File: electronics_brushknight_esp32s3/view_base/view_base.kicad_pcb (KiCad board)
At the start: 4 copper layers, 81.2 x 81.2 mm, 107 parts, among them J1 BLDC, J2 USB_C_Receptacle_USB2.0, J3 LCD, J4 A, J5 B, Q1 MMBT4403, Q2 UMH3N, U1 MT6701-CT, U10 ESP32-S3-WROOM-1-N8R8, U2 CP2102N-A02-GQFN28, U4 HX711, U5 TMC6300, U7 SN74LV1T34DBV, U8 VEML7700, U9 TS1117BCW33_RPG

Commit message: fixed bugs
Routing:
- net /LCD_SCK: track 19.4 -> 17.4 mm, vias 2 -> 1
- net +5V: track 20.2 -> 22.0 mm
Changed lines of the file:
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@@
     (fp_arc (start 3.878787 -15.522725) (mid 3.605918 -15.700082) (end 3.499999 -16.00781)
       (stroke (width 0.2) (type solid)) (layer "B.Fab"))
-    (fp_arc (start 3.878788 -15.522725) (mid 6.302306 -14.706494) (end 8.564827 -13.514574)
+    (fp_arc (start 3.878788 -15.522725) (mid 6.302306 -14.706493) (end 8.564827 -13.514574)
       (stroke (width 0.2) (type solid)) (layer "B.Fab"))
     (fp_arc (start 4.999999 -16.770509) (mid 7.404757 -15.856214) (end 9.649481 -14.599229)
@@
     (fp_arc (start 15.522725 3.878787) (mid 15.700082 3.605918) (end 16.00781 3.499999)
       (stroke (width 0.2) (type solid)) (layer "B.Fab"))
-    (fp_arc (start 15.522725 3.878788) (mid 14.706494 6.302306) (end 13.514574 8.564827)
+    (fp_arc (start 15.522725 3.878788) (mid 14.706493 6.302306) (end 13.514574 8.564827)
       (stroke (width 0.2) (type solid)) (layer "B.Fab"))
     (fp_arc (start 16.007811 -3.5) (mid 15.700077 -3.605911) (end 15.522725 -3.878787)
@@
   (segment (start 65.5 127) (end 72.75 127) (width 0.25) (layer "In1.Cu") (net 37))
   (segment (start 65.5 127) (end 67.5 127) (width 0.25) (layer "B.Cu") (net 37))
-  (via (at 65.5 125) (size 0.8) (drill 0.4) (layers "F.Cu" "B.Cu") (net 38))
   (via (at 77.25 133.5) (size 0.8) (drill 0.4) (layers "F.Cu" "B.Cu") (net 38))
   (segment (start 71.75 125) (end 67.5 125) (width 0.25) (layer "B.Cu") (net 38))
@@
   (segment (start 77.25 133.5) (end 73.25 133.5) (width 0.25) (layer "B.Cu") (net 38))
   (segment (start 72.5 132.75) (end 72.5 125.75) (width 0.25) (layer "B.Cu") (net 38))
-  (segment (start 65.5 125) (end 67.5 125) (width 0.25) (layer "B.Cu") (net 38))
   (segment (start 72.5 125.75) (end 71.75 125) (width 0.25) (layer "B.Cu") (net 38))
   (via (at 77.25 131) (size 0.8) (drill 0.4) (layers "F.Cu" "B.Cu") (net 39))
@@
   (segment (start 93.5 83.57586) (end 93.814763 83.890623) (width 0.65) (layer "F.Cu") (net 81))
   (segment (start 85.825142 88.25) (end 86.431129 88.855987) (width 0.4) (layer "F.Cu") (net 81))
+  (segment (start 69 108.775) (end 68.75 108.525) (width 0.15) (layer "F.Cu") (net 81))
   (segment (start 107.5 83.752753) (end 107.017427 84.235326) (width 0.65) (layer "F.Cu") (net 81))
   (segment (start 114.5 88.5) (end 114.175232 88.5) (width 0.4) (layer "F.Cu") (net 81))
@@
   (segment (start 92.5 116.247247) (end 92.982573 115.764674) (width 0.65) (layer "F.Cu") (net 81))
   (segment (start 106.5 116.42414) (end 106.185237 116.109377) (width 0.65) (layer "F.Cu") (net 81))
+  (segment (start 69 109.4) (end 69 108.775) (width 0.15) (layer "F.Cu") (net 81))
+  (segment (start 69 109.4) (end 69 109.6375) (width 0.15) (layer "F.Cu") (net 81))
   (segment (start 111.5 85.5) (end 111.5 85.825142) (width 0.4) (layer "F.Cu") (net 81))
   (segment (start 88.5 85.824768) (end 89.105236 86.430004) (width 0.4) (layer "F.Cu") (net 81))
@@
   (segment (start 114.5 111.5) (end 114.174858 111.5) (width 0.4) (layer "F.Cu") (net 81))
   (segment (start 111.5 85.825142) (end 110.894013 86.431129) (width 0.4) (layer "F.Cu") (net 81))
+  (segment (start 69 109.6375) (end 68.5875 110.05) (width 0.15) (layer "F.Cu") (net 81))
   (segment (start 85.824768 111.5) (end 86.430004 110.894764) (width 0.4) (layer "F.Cu") (net 81))
   (segment (start 83.25 92.5) (end 83.752753 92.5) (width 0.65) (layer "F.Cu") (net 81))

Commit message: devkit pcb preview
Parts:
- removed D1, D2, D3, D4, D5, D6, D7, D8: SK6812SIDE-A, cleaned footprints:SK6812-SIDE-A
- removed H4: MountHole, Holes:MountingHole_2.2mm_M2_ISO7380_Pad_NonVirtual
- removed Z5: dummy_keepouts, view_custom:ViewKeepouts3d
- added C100: 0.1uF, cleaned footprints:C_0402_1005Metric, F.Cu at (89.3, 122.8)
- added C101: 0.1uF, cleaned footprints:C_0402_1005Metric, F.Cu at (93.5, 124.3)
- added C11: 0.1uF, cleaned footprints:C_0402_1005Metric, F.Cu at (125.1, 97.8)
- added C30: 0.1uF, cleaned footprints:C_0402_1005Metric, F.Cu at (100.0, 125.2)
- added C31: 0.1uF, cleaned footprints:C_0402_1005Metric, F.Cu at (97.8, 74.9)
- added C32: 0.1uF, cleaned footprints:C_0402_1005Metric, F.Cu at (97.8, 125.1)
- added C33: 0.1uF, cleaned footprints:C_0402_1005Metric, F.Cu at (102.2, 74.9)
- added C34: 0.1uF, cleaned footprints:C_0402_1005Metric, F.Cu at (106.5, 124.3)
- added C35: 0.1uF, cleaned footprints:C_0402_1005Metric, F.Cu at (100.0, 74.8)
- added C36: 0.1uF, cleaned footprints:C_0402_1005Metric, F.Cu at (110.7, 122.9)
- added C37: 0.1uF, cleaned footprints:C_0402_1005Metric, F.Cu at (108.6, 76.3)
- added C38: 0.1uF, cleaned footprints:C_0402_1005Metric, F.Cu at (112.6, 78.2)
- added C39: 0.1uF, cleaned footprints:C_0402_1005Metric, F.Cu at (114.5, 120.7)
- added C40: 0.1uF, cleaned footprints:C_0402_1005Metric, F.Cu at (116.2, 80.7)
- added C41: 0.1uF, cleaned footprints:C_0402_1005Metric, F.Cu at (117.8, 117.8)
- added C42: 0.1uF, cleaned footprints:C_0402_1005Metric, F.Cu at (119.3, 83.8)
- added C43: 0.1uF, cleaned footprints:C_0402_1005Metric, F.Cu at (120.7, 114.5)
- added C44: 0.1uF, cleaned footprints:C_0402_1005Metric, F.Cu at (121.8, 87.4)
- added C45: 0.1uF, cleaned footprints:C_0402_1005Metric, F.Cu at (123.7, 91.4)
- added C46: 0.1uF, cleaned footprints:C_0402_1005Metric, F.Cu at (122.8, 110.7)
- added C47: 0.1uF, cleaned footprints:C_0402_1005Metric, F.Cu at (91.4, 76.3)
- added C48: 0.1uF, cleaned footprints:C_0402_1005Metric, F.Cu at (124.3, 106.5)
- added C49: 0.1uF, cleaned footprints:C_0402_1005Metric, F.Cu at (87.4, 78.2)
- added C50: 0.1uF, cleaned footprints:C_0402_1005Metric, F.Cu at (124.8, 104.4)
- added C51: 0.1uF, cleaned footprints:C_0402_1005Metric, F.Cu at (83.8, 80.7)
- added C52: 0.1uF, cleaned footprints:C_0402_1005Metric, F.Cu at (80.7, 83.8)
- added C53: 0.1uF, cleaned footprints:C_0402_1005Metric, F.Cu at (124.3, 93.5)
- added C54: 0.1uF, cleaned footprints:C_0402_1005Metric, F.Cu at (78.2, 87.4)
- added C55: 0.1uF, cleaned footprints:C_0402_1005Metric, F.Cu at (124.8, 95.6)
- added C56: 0.1uF, cleaned footprints:C_0402_1005Metric, F.Cu at (76.3, 91.4)
- added C57: 0.1uF, cleaned footprints:C_0402_1005Metric, F.Cu at (122.8, 89.3)
- added C58: 0.1uF, cleaned footprints:C_0402_1005Metric, F.Cu at (74.9, 97.8)
- added C59: 0.1uF, cleaned footprints:C_0402_1005Metric, F.Cu at (74.9, 102.2)
- added C60: 0.1uF, cleaned footprints:C_0402_1005Metric, F.Cu at (74.8, 100.0)
- added C61: 0.1uF, cleaned footprints:C_0402_1005Metric, F.Cu at (76.3, 108.6)
- added C62: 0.1uF, cleaned footprints:C_0402_1005Metric, F.Cu at (78.2, 112.6)
- added C63: 0.1uF, cleaned footprints:C_0402_1005Metric, F.Cu at (120.7, 85.5)
- added C64: 0.1uF, cleaned footprints:C_0402_1005Metric, F.Cu at (117.8, 82.2)
- added C65: 0.1uF, cleaned footprints:C_0402_1005Metric, F.Cu at (114.5, 79.3)
- added C66: 0.1uF, cleaned footprints:C_0402_1005Metric, F.Cu at (110.7, 77.2)
- added C67: 0.1uF, cleaned footprints:C_0402_1005Metric, F.Cu at (80.7, 116.2)
- added C68: 0.1uF, cleaned footprints:C_0402_1005Metric, F.Cu at (83.8, 119.3)
- added C69: 0.1uF, cleaned footprints:C_0402_1005Metric, F.Cu at (87.4, 121.8)
- added C70: 0.1uF, cleaned footprints:C_0402_1005Metric, F.Cu at (91.4, 123.7)
- added C71: 0.1uF, cleaned footprints:C_0402_1005Metric, F.Cu at (106.5, 75.6)
- added C72: 0.1uF, cleaned footprints:C_0402_1005Metric, F.Cu at (104.4, 75.2)
- added C73: 0.1uF, cleaned footprints:C_0402_1005Metric, F.Cu at (93.5, 75.6)
- added C74: 0.1uF, cleaned footprints:C_0402_1005Metric, F.Cu at (95.6, 75.2)
- added C75: 0.1uF, cleaned footprints:C_0402_1005Metric, F.Cu at (95.6, 124.8)
- added C76: 0.1uF, cleaned footprints:C_0402_1005Metric, F.Cu at (102.2, 125.1)
- added C77: 0.1uF, cleaned footprints:C_0402_1005Metric, F.Cu at (104.4, 124.8)
- added C78: 10uF, smd_clean:C_0603_1608Metric, F.Cu at (114.2, 62.2)
- added C79: 0.1uF, cleaned footprints:C_0402_1005Metric, F.Cu at (89.3, 77.2)
- added C80: 0.1uF, cleaned footprints:C_0402_1005Metric, F.Cu at (85.5, 79.4)
- added C81: 0.1uF, cleaned footprints:C_0402_1005Metric, F.Cu at (82.2, 82.2)
- added C82: 0.1uF, cleaned footprints:C_0402_1005Metric, F.Cu at (79.4, 85.5)
- added C83: 10uF, smd_clean:C_0603_1608Metric, F.Cu at (114.2, 67.3)
- added C84: 100nF, smd_clean:C_0603_1608Metric, F.Cu at (114.2, 68.9)
- added C88: 0.1uF, cleaned footprints:C_0402_1005Metric, F.Cu at (77.2, 89.3)
- added C90: 0.1uF, cleaned footprints:C_0402_1005Metric, F.Cu at (75.7, 93.5)
- added C92: 0.1uF, cleaned footprints:C_0402_1005Metric, F.Cu at (75.2, 95.6)
- added C94: 0.1uF, cleaned footprints:C_0402_1005Metric, F.Cu at (75.2, 104.4)
- added C95: 0.1uF, cleaned footprints:C_0402_1005Metric, F.Cu at (75.6, 106.5)
- added C96: 0.1uF, cleaned footprints:C_0402_1005Metric, F.Cu at (77.2, 110.7)
- added C97: 0.1uF, cleaned footprints:C_0402_1005Metric, F.Cu at (79.3, 114.5)
- added C98: 0.1uF, cleaned footprints:C_0402_1005Metric, F.Cu at (82.2, 117.8)
- added C99: 0.1uF, cleaned footprints:C_0402_1005Metric, F.Cu at (85.5, 120.6)
- added D10: SK6805, cleaned footprints:LED_SK6812_EC15_1.5x1.5mm, F.Cu at (97.7, 126.7)
- added D11: SK6805, cleaned footprints:LED_SK6812_EC15_1.5x1.5mm, F.Cu at (95.3, 126.3)
- added D12: SK6805, cleaned footprints:LED_SK6812_EC15_1.5x1.5mm, F.Cu at (93.1, 125.8)
- added D13: SK6805, cleaned footprints:LED_SK6812_EC15_1.5x1.5mm, F.Cu at (90.8, 125.1)
- added D14: SK6805, cleaned footprints:LED_SK6812_EC15_1.5x1.5mm, F.Cu at (88.7, 124.2)
- added D15: SK6805, cleaned footprints:LED_SK6812_EC15_1.5x1.5mm, F.Cu at (86.6, 123.2)
- added D16: SK6805, cleaned footprints:LED_SK6812_EC15_1.5x1.5mm, F.Cu at (84.7, 121.9)
- added D17: SK6805, cleaned footprints:LED_SK6812_EC15_1.5x1.5mm, F.Cu at (82.8, 120.5)
- added D18: SK6805, cleaned footprints:LED_SK6812_EC15_1.5x1.5mm, F.Cu at (81.1, 118.9)
- added D19: SK6805, cleaned footprints:LED_SK6812_EC15_1.5x1.5mm, F.Cu at (79.5, 117.2)
- added D20: SK6805, cleaned footprints:LED_SK6812_EC15_1.5x1.5mm, F.Cu at (78.1, 115.3)
- added D21: SK6805, cleaned footprints:LED_SK6812_EC15_1.5x1.5mm, F.Cu at (76.8, 113.4)
- added D22: SK6805, cleaned footprints:LED_SK6812_EC15_1.5x1.5mm, F.Cu at (75.8, 111.3)
- added D23: SK6805, cleaned footprints:LED_SK6812_EC15_1.5x1.5mm, F.Cu at (74.9, 109.2)
- added D24: SK6805, cleaned footprints:LED_SK6812_EC15_1.5x1.5mm, F.Cu at (74.2, 106.9)
- added D25: SK6805, cleaned footprints:LED_SK6812_EC15_1.5x1.5mm, F.Cu at (73.7, 104.6)
- added D26: SK6805, cleaned footprints:LED_SK6812_EC15_1.5x1.5mm, F.Cu at (73.4, 102.3)
- added D27: SK6805, cleaned footprints:LED_SK6812_EC15_1.5x1.5mm, F.Cu at (73.2, 100.0)
- added D28: SK6805, cleaned footprints:LED_SK6812_EC15_1.5x1.5mm, F.Cu at (73.4, 97.7)
- added D29: SK6805, cleaned footprints:LED_SK6812_EC15_1.5x1.5mm, F.Cu at (73.7, 95.4)
- added D30: SK6805, cleaned footprints:LED_SK6812_EC15_1.5x1.5mm, F.Cu at (74.2, 93.1)
- added D31: SK6805, cleaned footprints:LED_SK6812_EC15_1.5x1.5mm, F.Cu at (74.9, 90.9)
- added D32: SK6805, cleaned footprints:LED_SK6812_EC15_1.5x1.5mm, F.Cu at (75.8, 88.7)
- added D33: SK6805, cleaned footprints:LED_SK6812_EC15_1.5x1.5mm, F.Cu at (76.8, 86.6)
- added D34: SK6805, cleaned footprints:LED_SK6812_EC15_1.5x1.5mm, F.Cu at (78.1, 84.7)
- added D35: SK6805, cleaned footprints:LED_SK6812_EC15_1.5x1.5mm, F.Cu at (79.5, 82.8)
- added D36: SK6805, cleaned footprints:LED_SK6812_EC15_1.5x1.5mm, F.Cu at (81.1, 81.1)
- added D37: SK6805, cleaned footprints:LED_SK6812_EC15_1.5x1.5mm, F.Cu at (82.8, 79.5)
- added D38: SK6805, cleaned footprints:LED_SK6812_EC15_1.5x1.5mm, F.Cu at (84.7, 78.1)
- added D39: SK6805, cleaned footprints:LED_SK6812_EC15_1.5x1.5mm, F.Cu at (86.6, 76.8)
- added D40: SK6805, cleaned footprints:LED_SK6812_EC15_1.5x1.5mm, F.Cu at (88.7, 75.8)
- added D41: SK6805, cleaned footprints:LED_SK6812_EC15_1.5x1.5mm, F.Cu at (90.8, 74.9)
- added D42: SK6805, cleaned footprints:LED_SK6812_EC15_1.5x1.5mm, F.Cu at (109.2, 74.9)
- added D43: SK6805, cleaned footprints:LED_SK6812_EC15_1.5x1.5mm, F.Cu at (123.2, 86.6)
- added D44: SK6805, cleaned footprints:LED_SK6812_EC15_1.5x1.5mm, F.Cu at (126.3, 104.6)
- added D45: SK6805, cleaned footprints:LED_SK6812_EC15_1.5x1.5mm, F.Cu at (93.1, 74.2)
- added D46: SK6805, cleaned footprints:LED_SK6812_EC15_1.5x1.5mm, F.Cu at (111.3, 75.8)
- added D47: SK6805, cleaned footprints:LED_SK6812_EC15_1.5x1.5mm, F.Cu at (124.2, 88.7)
- added D48: SK6805, cleaned footprints:LED_SK6812_EC15_1.5x1.5mm, F.Cu at (125.8, 106.9)
- added D49: SK6805, cleaned footprints:LED_SK6812_EC15_1.5x1.5mm, F.Cu at (95.4, 73.7)
- added D50: SK6805, cleaned footprints:LED_SK6812_EC15_1.5x1.5mm, F.Cu at (113.4, 76.8)
- added D51: SK6805, cleaned footprints:LED_SK6812_EC15_1.5x1.5mm, F.Cu at (125.1, 90.9)
- added D52: SK6805, cleaned footprints:LED_SK6812_EC15_1.5x1.5mm, F.Cu at (125.1, 109.2)
- added D53: SK6805, cleaned footprints:LED_SK6812_EC15_1.5x1.5mm, F.Cu at (97.7, 73.4)
- added D54: SK6805, cleaned footprints:LED_SK6812_EC15_1.5x1.5mm, F.Cu at (115.3, 78.1)
- added D55: SK6805, cleaned footprints:LED_SK6812_EC15_1.5x1.5mm, F.Cu at (125.8, 93.1)
- added D56: SK6805, cleaned footprints:LED_SK6812_EC15_1.5x1.5mm, F.Cu at (124.2, 111.3)
- added D57: SK6805, cleaned footprints:LED_SK6812_EC15_1.5x1.5mm, F.Cu at (100.0, 73.2)
- added D58: SK6805, cleaned footprints:LED_SK6812_EC15_1.5x1.5mm, F.Cu at (117.2, 79.5)
- added D59: SK6805, cleaned footprints:LED_SK6812_EC15_1.5x1.5mm, F.Cu at (126.3, 95.4)
- added D60: SK6805, cleaned footprints:LED_SK6812_EC15_1.5x1.5mm, F.Cu at (123.2, 113.4)
- added D61: SK6805, cleaned footprints:LED_SK6812_EC15_1.5x1.5mm, F.Cu at (102.3, 73.4)
- added D62: SK6805, cleaned footprints:LED_SK6812_EC15_1.5x1.5mm, F.Cu at (118.9, 81.1)
- added D63: SK6805, cleaned footprints:LED_SK6812_EC15_1.5x1.5mm, F.Cu at (126.6, 97.7)
- added D64: SK6805, cleaned footprints:LED_SK6812_EC15_1.5x1.5mm, F.Cu at (121.9, 115.3)
- added D65: SK6805, cleaned footprints:LED_SK6812_EC15_1.5x1.5mm, F.Cu at (104.7, 73.7)
- added D66: SK6805, cleaned footprints:LED_SK6812_EC15_1.5x1.5mm, F.Cu at (120.5, 82.8)
- added D67: SK6805, cleaned footprints:LED_SK6812_EC15_1.5x1.5mm, F.Cu at (126.7, 100.0)
- added D68: SK6805, cleaned footprints:LED_SK6812_EC15_1.5x1.5mm, F.Cu at (120.5, 117.2)
- added D69: SK6805, cleaned footprints:LED_SK6812_EC15_1.5x1.5mm, F.Cu at (106.9, 74.2)
- added D70: SK6805, cleaned footprints:LED_SK6812_EC15_1.5x1.5mm, F.Cu at (121.9, 84.7)
- added D71: SK6805, cleaned footprints:LED_SK6812_EC15_1.5x1.5mm, F.Cu at (126.7, 102.3)
- added D72: SK6805, cleaned footprints:LED_SK6812_EC15_1.5x1.5mm, F.Cu at (118.9, 118.9)
- added D73: SK6805, cleaned footprints:LED_SK6812_EC15_1.5x1.5mm, F.Cu at (117.2, 120.5)
- added D74: SK6805, cleaned footprints:LED_SK6812_EC15_1.5x1.5mm, F.Cu at (115.3, 121.9)
- added D75: SK6805, cleaned footprints:LED_SK6812_EC15_1.5x1.5mm, F.Cu at (113.4, 123.2)
- added D76: SK6805, cleaned footprints:LED_SK6812_EC15_1.5x1.5mm, F.Cu at (111.3, 124.2)
- added D77: SK6805, cleaned footprints:LED_SK6812_EC15_1.5x1.5mm, F.Cu at (109.1, 125.1)
- added D78: SK6805, cleaned footprints:LED_SK6812_EC15_1.5x1.5mm, F.Cu at (106.9, 125.8)
- added D79: SK6805, cleaned footprints:LED_SK6812_EC15_1.5x1.5mm, F.Cu at (104.7, 126.3)
- added D80: SK6805, cleaned footprints:LED_SK6812_EC15_1.5x1.5mm, F.Cu at (102.3, 126.7)
- added D9: SK6805, cleaned footprints:LED_SK6812_EC15_1.5x1.5mm, F.Cu at (100.0, 126.8)
- added J6: LCD - FPC, screen_connector:Amphenol FCI FPC 8 pin 0.5 pitch, B.Cu at (83.5, 116.6)
- added J7: Conn_01x04_Socket, cleaned footprints:JST_SH_SM04B-SRSS-TB_1x04-1MP_P1.00mm_Horizontal, B.Cu at (133.2, 62.9)
- added J8: Conn_01x04_Socket, cleaned footprints:JST_SH_SM04B-SRSS-TB_1x04-1MP_P1.00mm_Horizontal, B.Cu at (125.4, 62.9)
- added J9: Conn_01x04_Socket, cleaned footprints:JST_SH_SM04B-SRSS-TB_1x04-1MP_P1.00mm_Horizontal, B.Cu at (117.6, 62.9)
- added Q3: BSS138, smd_clean:SOT-23, F.Cu at (108.2, 63.8)
- added R23: 10K, smd_clean:R_0603_1608Metric, F.Cu at (105.5, 67.2)
- added R24: 10K, smd_clean:R_0603_1608Metric, F.Cu at (105.4, 63.9)
- added R25: 10K, smd_clean:R_0603_1608Metric, F.Cu at (94.8, 64.2)
- added R26: 10K, smd_clean:R_0603_1608Metric, F.Cu at (111.2, 67.1)
- added R27: 10K, smd_clean:R_0603_1608Metric, F.Cu at (111.2, 64.0)
- added R28: 10k, cleaned footprints:R_0603_1608Metric, F.Cu at (84.2, 136.7)
- added REF**: fpc_wire_hole_6mm, view_custom:fpc_wire_hole_6mm, F.Cu at (97.2, 102.8)
- added REF**: seedlabs_smartknob, seedlabs:seedlabs_smartknob, F.Cu at (128.5, 68.0)
- added SW1: RST, smd_clean:SW_SPST_PTS810, B.Cu at (79.8, 132.2)
- added SW2: Boot, smd_clean:SW_SPST_PTS810, B.Cu at (75.8, 132.2)
- added TP17: IO40, cleaned footprints:TestPoint_Pad_D2.0mm_ValueSilk, B.Cu at (116.2, 138.2)
- added TP18: IO41, cleaned footprints:TestPoint_Pad_D2.0mm_ValueSilk, B.Cu at (113.2, 138.2)
- added TP19: IO42, cleaned footprints:TestPoint_Pad_D2.0mm_ValueSilk, B.Cu at (110.2, 138.2)
- added TP20: IO45, cleaned footprints:TestPoint_Pad_D2.0mm_ValueSilk, B.Cu at (119.2, 138.2)
- added TP21: IO46, cleaned footprints:TestPoint_Pad_D2.0mm_ValueSilk, B.Cu at (128.2, 138.2)
- added TP22: IO47, cleaned footprints:TestPoint_Pad_D2.0mm_ValueSilk, B.Cu at (125.2, 138.2)
- added TP23: IO48, cleaned footprints:TestPoint_Pad_D2.0mm_ValueSilk, B.Cu at (122.2, 138.2)
- added U3: VL53L0CXV0DH_1, smd_clean:LGA12_1, F.Cu at (100.0, 65.5)
- added U6: LP5907MFX-2.8, cleaned footprints:SOT-23-5, F.Cu at (114.2, 64.8)
- C1, C2, C29, C3, C4, C5, C6, C7, C8: footprint cleaned footprints:C_0603_1608Metric -> cleaned footprints:C_0402_1005Metric
- Q2: value UMH3N -> BSS138; footprint cleaned footprints:SOT-363_SC-70-6 -> smd_clean:SOT-23
- R22: value 1K -> 10K; footprint cleaned footprints:R_0603_1608Metric -> smd_clean:R_0603_1608Metric
- TP1, TP10, TP11, TP12, TP13, TP14, TP15, TP16, TP3, TP4, TP5, TP6, TP7, TP8, TP9: footprint Modified:TestPoint_Pad_D2.0mm_ValueSilk -> cleaned footprints:TestPoint_Pad_D2.0mm_ValueSilk
- TP2: value 3.3v -> 3V3; footprint Modified:TestPoint_Pad_D2.0mm_ValueSilk -> cleaned footprints:TestPoint_Pad_D2.0mm_ValueSilk
- U2: value CP2102N-A02-GQFN28 -> USBLC6-2SC6; footprint cp2102:Silicon_Labs-CP2102N-A02-GQFN28-IPC_A -> smd_clean:SOT-23-6
- moved Q2 74.2 mm to (108.2, 67.3), turned to 0 degrees
- moved R22 64.5 mm to (94.8, 66.8), turned to 180 degrees
- moved R14 60.8 mm to (64.2, 114.1)
- moved R13 57.8 mm to (65.8, 114.1)
- moved C8 41.1 mm to (125.1, 102.2), turned to 85 degrees
- moved C7 38.1 mm to (125.2, 100.0), turned to 90 degrees
- moved U7 34.0 mm to (89.6, 136.8)
- moved C29 33.9 mm to (89.6, 134.4), turned to 180 degrees
- moved TP12 29.9 mm to (83.8, 138.2)
- moved C1 26.3 mm to (108.6, 123.7), turned to 20 degrees
- moved C6 26.3 mm to (123.7, 108.6), turned to 70 degrees
- moved C2 24.2 mm to (112.6, 121.8), turned to 30 degrees
- moved C5 24.2 mm to (121.8, 112.6), turned to 60 degrees
- moved TP15 23.8 mm to (67.8, 138.2)
- moved TP9 22.4 mm to (67.5, 104.5)
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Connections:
- Q2 pad 1: /RTS -> +2V8
- Q2 pad 2: /DTR -> SCL_2.8
- Q2 pad 3: /ESP32_BOOT -> SCL
- R13 pad 2: /SDA -> SDA
- R14 pad 2: /SCL -> SCL
- R22 pad 1: +3V3 -> Net-(U3-XSHUT)
- R22 pad 2: Net-(U2-~{RST}) -> +2V8
- TP4 pad 1: /SDA -> SDA
- TP5 pad 1: /SCL -> SCL
- U10 pad 10: /TMC_VL -> /TMC_WH
- U10 pad 11: /TMC_WL -> /TMC_VH
- U10 pad 12: /SCL -> /TMC_UH
- U10 pad 13: /TMC_UL -> /ESP_USB_D-
- U10 pad 14: /TMC_UH -> /ESP_USB_D+
- U10 pad 16: unconnected-(U10-IO46-Pad16) -> Net-(U10-IO46)
- U10 pad 18: unconnected-(U10-IO10-Pad18) -> /LCD_RST
- U10 pad 19: unconnected-(U10-IO11-Pad19) -> /MAG_CSN
- U10 pad 20: /TMC_WH -> /LED_DATA_3V3
- U10 pad 22: /MAG_CSN -> /MAG_DO
- U10 pad 23: /TMC_VH -> /STRAIN_DO
- U10 pad 24: unconnected-(U10-IO47-Pad24) -> Net-(U10-IO47)
- U10 pad 25: unconnected-(U10-IO48-Pad25) -> Net-(U10-IO48)
- U10 pad 26: unconnected-(U10-IO45-Pad26) -> Net-(U10-IO45)
- U10 pad 29: /TMC_DIAG -> unconnected-(U10-IO36-Pad29)
- U10 pad 30: /MAG_DO -> unconnected-(U10-IO37-Pad30)
- U10 pad 31: /STRAIN_DO -> SCL
- U10 pad 32: unconnected-(U10-IO39-Pad32) -> SDA
- U10 pad 33: unconnected-(U10-IO40-Pad33) -> Net-(U10-IO40)
- U10 pad 34: unconnected-(U10-IO41-Pad34) -> Net-(U10-IO41)
- U10 pad 35: unconnected-(U10-IO42-Pad35) -> Net-(U10-IO42)
- U10 pad 6: /LCD_RST -> /TMC_DIAG
- U10 pad 7: /LED_DATA_3V3 -> /TMC_VL
- U10 pad 8: /SDA -> /TMC_WL
- U10 pad 9: unconnected-(U10-IO16-Pad9) -> /TMC_UL
- U2 pad 1: unconnected-(U2-DCD-Pad1) -> /USB_D-
- U2 pad 2: unconnected-(U2-~{RI}/CLK-Pad2) -> GND
- U2 pad 3: GND -> /USB_D+
- U2 pad 4: /USB_D+ -> /ESP_USB_D+
- U2 pad 5: /USB_D- -> +5V
- U2 pad 6: +3V3 -> /ESP_USB_D-
- U8 pad 1: /SCL -> SCL
- U8 pad 4: /SDA -> SDA
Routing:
- net SCL: track 0.00 -> 190.7 mm, vias 0 -> 7
- net SDA: track 0.00 -> 183.0 mm, vias 0 -> 8
- net /SCL: track 139.1 -> 0.00 mm, vias 3 -> 0
- net /SDA: track 128.4 -> 0.00 mm, vias 3 -> 0
- net Net-(U10-IO46): track 0.00 -> 104.6 mm, vias 0 -> 2
- net Net-(U10-IO47): track 0.00 -> 93.0 mm, vias 0 -> 2
- net Net-(U10-IO48): track 0.00 -> 91.2 mm, vias 0 -> 2
- net Net-(U10-IO45): track 0.00 -> 87.4 mm, vias 0 -> 2
- net Net-(U10-IO40): track 0.00 -> 76.1 mm, vias 0 -> 2
- net Net-(U10-IO41): track 0.00 -> 72.2 mm, vias 0 -> 2
- net Net-(U10-IO42): track 0.00 -> 68.0 mm, vias 0 -> 2
- net +5V: track 22.0 -> 79.1 mm, vias 24 -> 78
- net GND: track 27.8 -> 67.4 mm, vias 30 -> 76
- net /MAG_DO: track 88.3 -> 53.8 mm, vias 3 -> 2
- net /USB_SERIAL_RXI: track 41.5 -> 14.0 mm
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- added copper zone on In2.Cu, net +2V8
- added copper zone on In1.Cu, net GND
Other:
- outline, holes or cut-outs redrawn
- board text added: "01"
- board text added: "5"
- board text added: "DEVKIT"
- board text added: "G"
- board text added: "G - Ground 5 - VCC 5V D - SDA C - SCL"
- board text added: "RST"
- board text added: "SUBJECT"
- board text added: "v0.1"
- board text removed: "Base PCB esp32s3"
- board text removed: "DATE: ${COMMIT_DATE_LONG} COMMIT: ${COMMIT_HASH}"
- board text removed: "SmartKnob View"
- board text removed: "power"

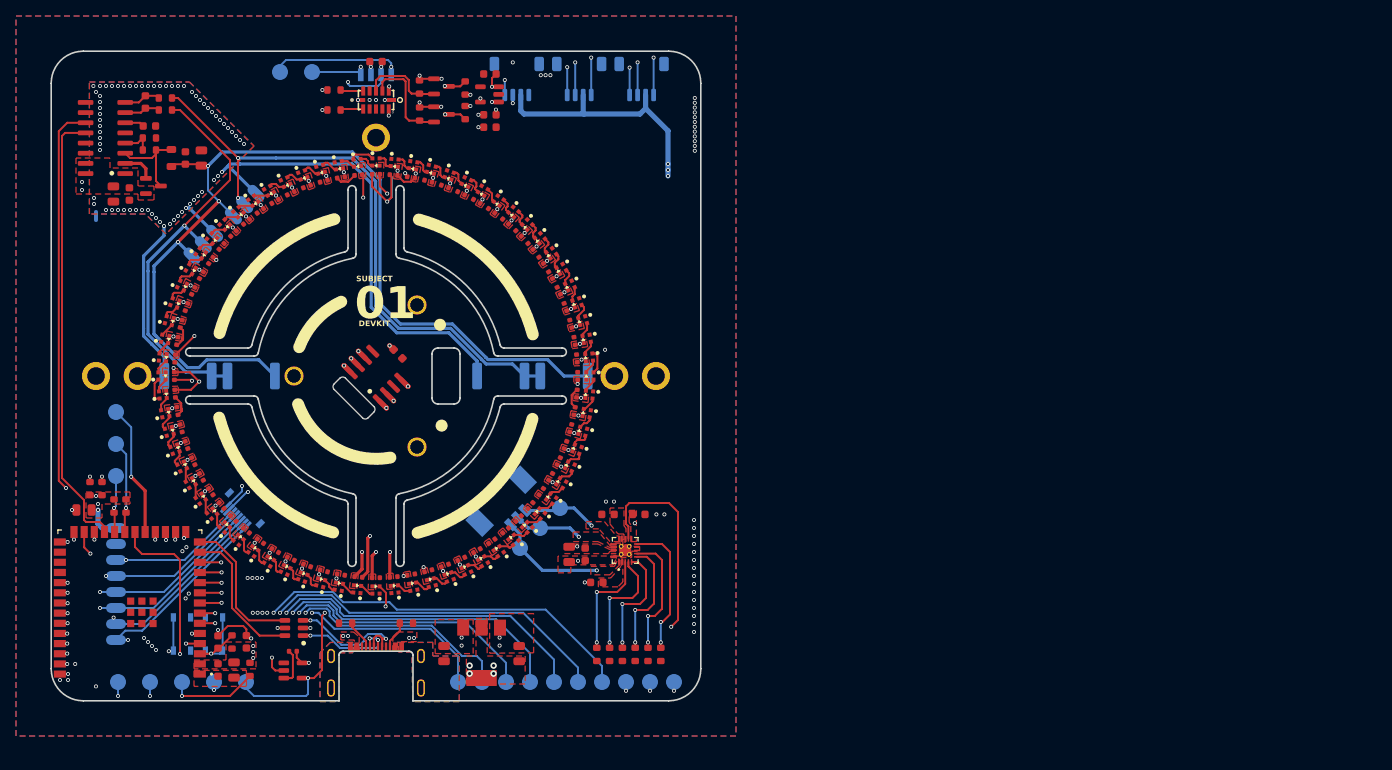
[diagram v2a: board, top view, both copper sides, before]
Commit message: Revert "DevKit PCB"
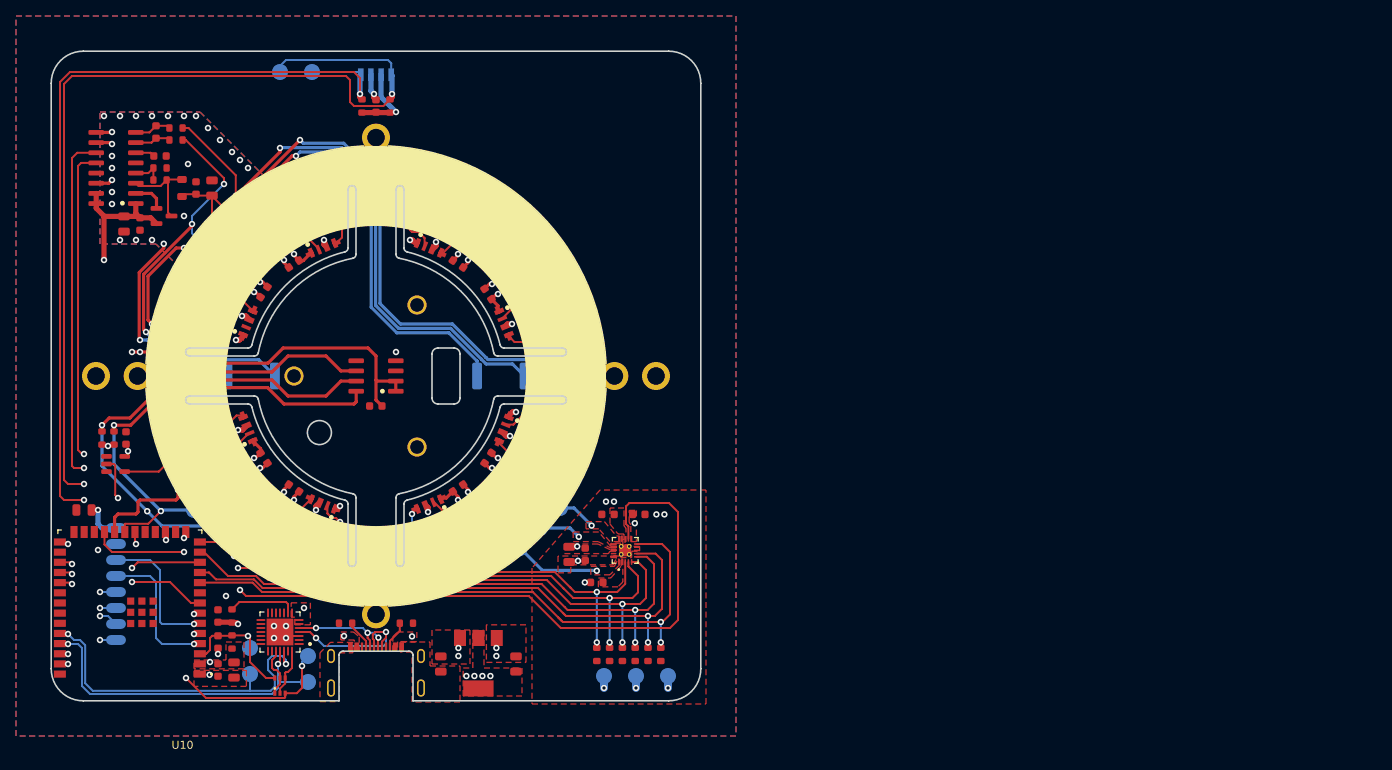
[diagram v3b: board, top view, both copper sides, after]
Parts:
- removed C100, C101, C30, C31, C32, C33, C34, C35, C36, C37, C38, C39, C40, C41, C42, C43, C44, C45, C46, C47, C48, C49, C50, C51, C52, C53, C54, C55, C56, C57, C58, C59, C60, C61, C62, C63, C64, C65, C66, C67, C68, C69, C70, C71, C72, C73, C74, C75, C76, C77, C79, C80, C81, C82, C88, C90, C92, C94, C95, C96, C97, C98, C99: 0.1uF, cleaned footprints:C_0402_1005Metric
- removed the C11 at (125.1, 97.8)
- removed C78, C83: 10uF, smd_clean:C_0603_1608Metric
- removed C84: 100nF, smd_clean:C_0603_1608Metric
- removed D10, D11, D12, D13, D14, D15, D16, D17, D18, D19, D20, D21, D22, D23, D24, D25, D26, D27, D28, D29, D30, D31, D32, D33, D34, D35, D36, D37, D38, D39, D40, D41, D42, D43, D44, D45, D46, D47, D48, D49, D50, D51, D52, D53, D54, D55, D56, D57, D58, D59, D60, D61, D62, D63, D64, D65, D66, D67, D68, D69, D70, D71, D72, D73, D74, D75, D76, D77, D78, D79, D80, D9: SK6805, cleaned footprints:LED_SK6812_EC15_1.5x1.5mm
- removed J6: LCD - FPC, screen_connector:Amphenol FCI FPC 8 pin 0.5 pitch
- removed J7, J8, J9: Conn_01x04_Socket, cleaned footprints:JST_SH_SM04B-SRSS-TB_1x04-1MP_P1.00mm_Horizontal
- removed Q3: BSS138, smd_clean:SOT-23
- removed R23, R24, R25, R26, R27: 10K, smd_clean:R_0603_1608Metric
- removed R28: 10k, cleaned footprints:R_0603_1608Metric
- removed REF**: fpc_wire_hole_6mm, view_custom:fpc_wire_hole_6mm
- removed REF**: seedlabs_smartknob, seedlabs:seedlabs_smartknob
- removed SW1: RST, smd_clean:SW_SPST_PTS810
- removed SW2: Boot, smd_clean:SW_SPST_PTS810
- removed TP17: IO40, cleaned footprints:TestPoint_Pad_D2.0mm_ValueSilk
- removed TP18: IO41, cleaned footprints:TestPoint_Pad_D2.0mm_ValueSilk
- removed TP19: IO42, cleaned footprints:TestPoint_Pad_D2.0mm_ValueSilk
- removed TP20: IO45, cleaned footprints:TestPoint_Pad_D2.0mm_ValueSilk
- removed TP21: IO46, cleaned footprints:TestPoint_Pad_D2.0mm_ValueSilk
- removed TP22: IO47, cleaned footprints:TestPoint_Pad_D2.0mm_ValueSilk
- removed TP23: IO48, cleaned footprints:TestPoint_Pad_D2.0mm_ValueSilk
- removed U3: VL53L0CXV0DH_1, smd_clean:LGA12_1
- removed U6: LP5907MFX-2.8, cleaned footprints:SOT-23-5
- added D1: SK6812SIDE-A, cleaned footprints:SK6812-SIDE-A, F.Cu at (83.4, 104.9)
- added D2: SK6812SIDE-A, cleaned footprints:SK6812-SIDE-A, F.Cu at (91.7, 115.2)
- added D3: SK6812SIDE-A, cleaned footprints:SK6812-SIDE-A, F.Cu at (104.9, 116.6)
- added D4: SK6812SIDE-A, cleaned footprints:SK6812-SIDE-A, F.Cu at (115.2, 108.3)
- added D5: SK6812SIDE-A, cleaned footprints:SK6812-SIDE-A, F.Cu at (116.6, 95.1)
- added D6: SK6812SIDE-A, cleaned footprints:SK6812-SIDE-A, F.Cu at (108.3, 84.8)
- added D7: SK6812SIDE-A, cleaned footprints:SK6812-SIDE-A, F.Cu at (95.1, 83.4)
- added D8: SK6812SIDE-A, cleaned footprints:SK6812-SIDE-A, F.Cu at (84.8, 91.7)
- added H4: MountHole, Holes:MountingHole_2.2mm_M2_ISO7380_Pad_NonVirtual, F.Cu at (100.0, 129.8)
- added Z5: dummy_keepouts, view_custom:ViewKeepouts3d, F.Cu at (100.0, 100.0)
- C1, C2, C29, C3, C4, C5, C6, C7, C8: footprint cleaned footprints:C_0402_1005Metric -> cleaned footprints:C_0603_1608Metric
- Q2: value BSS138 -> UMH3N; footprint smd_clean:SOT-23 -> cleaned footprints:SOT-363_SC-70-6
- R22: value 10K -> 1K; footprint smd_clean:R_0603_1608Metric -> cleaned footprints:R_0603_1608Metric
- TP1, TP10, TP11, TP12, TP13, TP14, TP15, TP16, TP3, TP4, TP5, TP6, TP7, TP8, TP9: footprint cleaned footprints:TestPoint_Pad_D2.0mm_ValueSilk -> Modified:TestPoint_Pad_D2.0mm_ValueSilk
- TP2: value 3V3 -> 3.3v; footprint cleaned footprints:TestPoint_Pad_D2.0mm_ValueSilk -> Modified:TestPoint_Pad_D2.0mm_ValueSilk
- U2: value USBLC6-2SC6 -> CP2102N-A02-GQFN28; footprint smd_clean:SOT-23-6 -> cp2102:Silicon_Labs-CP2102N-A02-GQFN28-IPC_A
- moved Q2 74.2 mm to (88.0, 138.7), turned to 90 degrees
- moved R22 64.5 mm to (82.0, 130.0), turned to 90 degrees
- moved R14 60.8 mm to (101.8, 66.2)
- moved R13 57.8 mm to (98.2, 66.2)
- moved C8 41.1 mm to (86.0, 89.5), turned to -123.8 degrees
- moved C7 38.1 mm to (89.8, 86.0), turned to 33.7 degrees
- moved U7 34.0 mm to (67.5, 111.0)
- moved C29 33.9 mm to (68.8, 107.8), turned to 90 degrees
- moved TP12 29.9 mm to (80.5, 108.5)
- moved C1 26.3 mm to (86.0, 110.2), turned to 123.7 degrees
- moved C6 26.3 mm to (110.2, 86.0), turned to 146.2 degrees
- moved C2 24.2 mm to (89.8, 114.0), turned to -33.8 degrees
- moved C5 24.2 mm to (114.0, 89.8), turned to -56.3 degrees
- moved TP15 23.8 mm to (91.5, 138.2)
- moved TP9 22.4 mm to (86.2, 116.8)
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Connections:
- Q2 pad 1: +2V8 -> /RTS
- Q2 pad 2: SCL_2.8 -> /DTR
- Q2 pad 3: SCL -> /ESP32_BOOT
- R13 pad 2: SDA -> /SDA
- R14 pad 2: SCL -> /SCL
- R22 pad 1: Net-(U3-XSHUT) -> +3V3
- R22 pad 2: +2V8 -> Net-(U2-~{RST})
- TP4 pad 1: SDA -> /SDA
- TP5 pad 1: SCL -> /SCL
- U10 pad 10: /TMC_WH -> /TMC_VL
- U10 pad 11: /TMC_VH -> /TMC_WL
- U10 pad 12: /TMC_UH -> /SCL
- U10 pad 13: /ESP_USB_D- -> /TMC_UL
- U10 pad 14: /ESP_USB_D+ -> /TMC_UH
- U10 pad 16: Net-(U10-IO46) -> unconnected-(U10-IO46-Pad16)
- U10 pad 18: /LCD_RST -> unconnected-(U10-IO10-Pad18)
- U10 pad 19: /MAG_CSN -> unconnected-(U10-IO11-Pad19)
- U10 pad 20: /LED_DATA_3V3 -> /TMC_WH
- U10 pad 22: /MAG_DO -> /MAG_CSN
- U10 pad 23: /STRAIN_DO -> /TMC_VH
- U10 pad 24: Net-(U10-IO47) -> unconnected-(U10-IO47-Pad24)
- U10 pad 25: Net-(U10-IO48) -> unconnected-(U10-IO48-Pad25)
- U10 pad 26: Net-(U10-IO45) -> unconnected-(U10-IO45-Pad26)
- U10 pad 29: unconnected-(U10-IO36-Pad29) -> /TMC_DIAG
- U10 pad 30: unconnected-(U10-IO37-Pad30) -> /MAG_DO
- U10 pad 31: SCL -> /STRAIN_DO
- U10 pad 32: SDA -> unconnected-(U10-IO39-Pad32)
- U10 pad 33: Net-(U10-IO40) -> unconnected-(U10-IO40-Pad33)
- U10 pad 34: Net-(U10-IO41) -> unconnected-(U10-IO41-Pad34)
- U10 pad 35: Net-(U10-IO42) -> unconnected-(U10-IO42-Pad35)
- U10 pad 6: /TMC_DIAG -> /LCD_RST
- U10 pad 7: /TMC_VL -> /LED_DATA_3V3
- U10 pad 8: /TMC_WL -> /SDA
- U10 pad 9: /TMC_UL -> unconnected-(U10-IO16-Pad9)
- U2 pad 1: /USB_D- -> unconnected-(U2-DCD-Pad1)
- U2 pad 2: GND -> unconnected-(U2-~{RI}/CLK-Pad2)
- U2 pad 3: /USB_D+ -> GND
- U2 pad 4: /ESP_USB_D+ -> /USB_D+
- U2 pad 5: +5V -> /USB_D-
- U2 pad 6: /ESP_USB_D- -> +3V3
- U8 pad 1: SCL -> /SCL
- U8 pad 4: SDA -> /SDA
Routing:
- net SCL: track 190.7 -> 0.00 mm, vias 7 -> 0
- net SDA: track 183.0 -> 0.00 mm, vias 8 -> 0
- net /SCL: track 0.00 -> 139.1 mm, vias 0 -> 3
- net /SDA: track 0.00 -> 128.4 mm, vias 0 -> 3
- net Net-(U10-IO46): track 104.6 -> 0.00 mm, vias 2 -> 0
- net Net-(U10-IO47): track 93.0 -> 0.00 mm, vias 2 -> 0
- net Net-(U10-IO48): track 91.2 -> 0.00 mm, vias 2 -> 0
- net Net-(U10-IO45): track 87.4 -> 0.00 mm, vias 2 -> 0
- net Net-(U10-IO40): track 76.1 -> 0.00 mm, vias 2 -> 0
- net Net-(U10-IO41): track 72.2 -> 0.00 mm, vias 2 -> 0
- net Net-(U10-IO42): track 68.0 -> 0.00 mm, vias 2 -> 0
- net +5V: track 79.1 -> 22.0 mm, vias 78 -> 24
- net GND: track 67.4 -> 27.8 mm, vias 76 -> 30
- net /MAG_DO: track 53.8 -> 88.3 mm, vias 2 -> 3
- net /USB_SERIAL_RXI: track 14.0 -> 41.5 mm
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- removed copper zone on In2.Cu, net +2V8
- removed copper zone on In1.Cu, net GND
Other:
- outline, holes or cut-outs redrawn
- board text added: "Base PCB esp32s3"
- board text added: "DATE: ${COMMIT_DATE_LONG} COMMIT: ${COMMIT_HASH}"
- board text added: "SmartKnob View"
- board text added: "power"
- board text removed: "01"
- board text removed: "5"
- board text removed: "DEVKIT"
- board text removed: "G"
- board text removed: "G - Ground 5 - VCC 5V D - SDA C - SCL"
- board text removed: "RST"
- board text removed: "SUBJECT"
- board text removed: "v0.1"

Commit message: wip new display
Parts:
- added J6: LCD - FPC, screen_connector:Amphenol FCI FPC 8 pin 0.5 pitch, B.Cu at (83.5, 116.6)
- moved TP9 9.98 mm to (77.0, 113.0)
- moved TP10 5.67 mm to (73.0, 113.0)
- moved TP11 5.51 mm to (75.0, 116.5)
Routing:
- net /MAG_CSN: track 61.4 -> 49.4 mm
- net /MAG_DO: track 88.3 -> 79.4 mm
- net /MAG_CLK: track 58.5 -> 54.5 mm
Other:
- outline, holes or cut-outs redrawn
